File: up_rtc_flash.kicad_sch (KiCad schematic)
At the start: 8 parts, among them J1 EduboardV2 PCIE UP Board Conn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

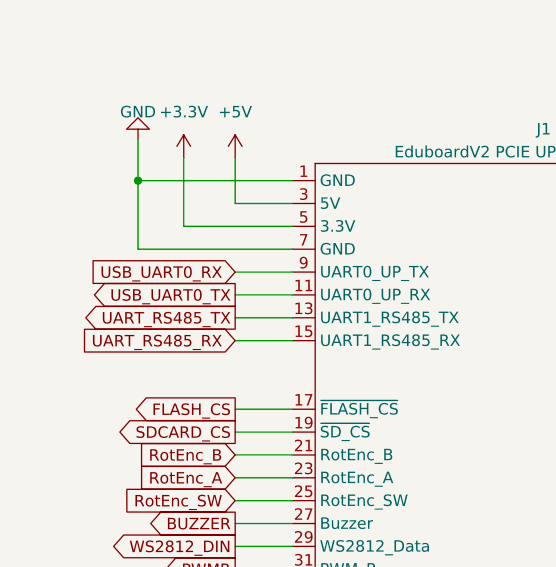
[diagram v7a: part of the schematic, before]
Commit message: Sort out RX/TX problems, improve DAC Circuits, Improve Board Text, switch out certain solder-jumpers with resistors
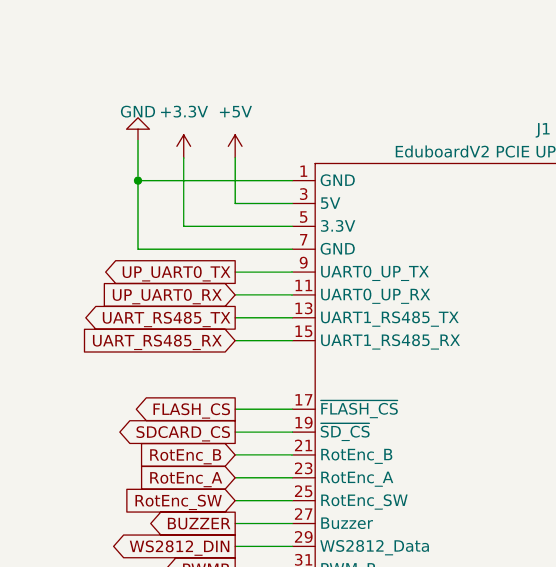
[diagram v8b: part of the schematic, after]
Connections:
- net USB_UART0_RX renamed UP_UART0_TX
- net USB_UART0_TX renamed UP_UART0_RX
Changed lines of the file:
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@@
     )
   )
-  (global_label "USB_UART0_TX" (shape output) (at 38.1 60.96 180) (fields_autoplaced)
+  (global_label "UP_UART0_RX" (shape input) (at 38.1 60.96 180) (fields_autoplaced)
     (effects (font (size 1.27 1.27)) (justify right))
-    (property "Intersheetrefs" "${INTERSHEET_REFS}" (at 21.4057 60.96 0)
+    (property "Intersheetrefs" "${INTERSHEET_REFS}" (at 22.3128 60.96 0)
       (effects (font (size 1.27 1.27)) (justify right) hide)
     )
@@
     )
   )
-  (global_label "USB_UART0_RX" (shape input) (at 38.1 58.42 180) (fields_autoplaced)
+  (global_label "UP_UART0_TX" (shape output) (at 38.1 58.42 180) (fields_autoplaced)
     (effects (font (size 1.27 1.27)) (justify right))
-    (property "Intersheetrefs" "${INTERSHEET_REFS}" (at 21.1033 58.42 0)
+    (property "Intersheetrefs" "${INTERSHEET_REFS}" (at 22.6152 58.42 0)
       (effects (font (size 1.27 1.27)) (justify right) hide)
     )
